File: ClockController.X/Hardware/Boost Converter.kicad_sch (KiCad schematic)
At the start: 9 parts, among them J2 HDR-1X2H, Q2 FDD7N25LZTM, Q3 MMBT2222A-TP, Q4 MMBT2907ALT1G

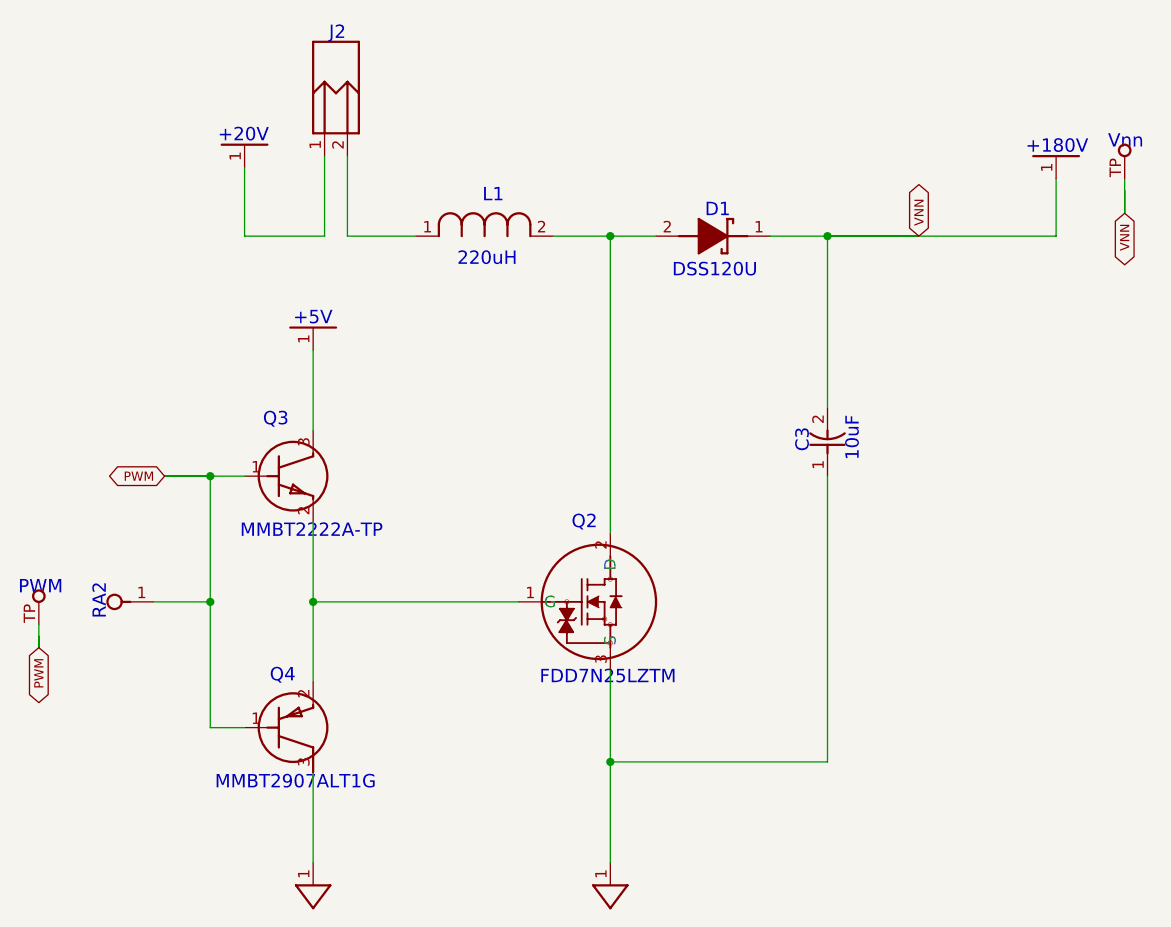
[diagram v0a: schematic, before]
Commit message: Replace the imported objects with native kicad equivalents
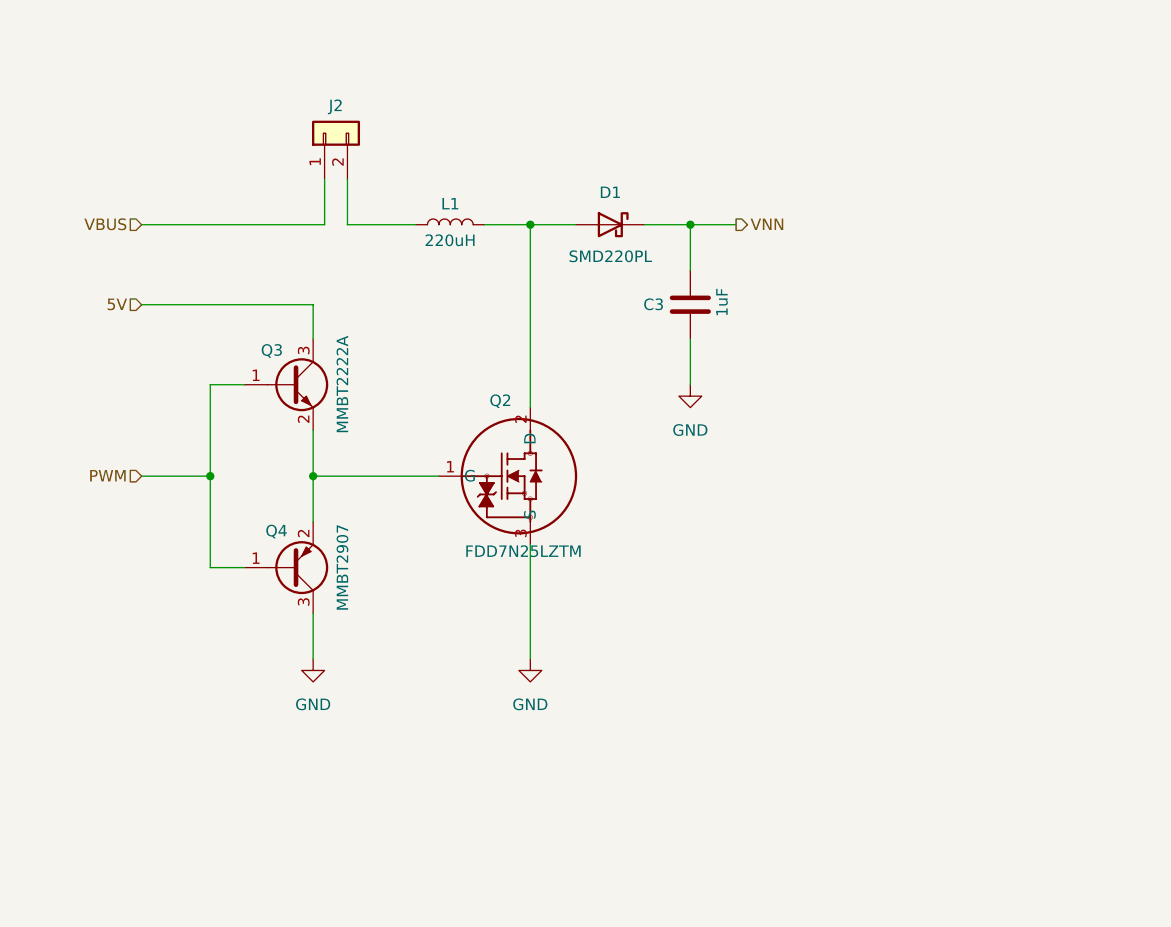
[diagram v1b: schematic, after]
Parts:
- removed PWM0, Vnn0: Most Density, Clock Controller:TP_1.25MM, symbol Clock Controller-eagle-import:TP_1.25MM
- C3: value 10uF -> 1uF; symbol Clock Controller-eagle-import:CAP_1206 -> Device:C
- D1: symbol Clock Controller-eagle-import:DSS120U -> Device:D_Schottky
- J2: symbol Clock Controller-eagle-import:HDR-1X2H -> Connector_Generic:Conn_01x02
- L1: footprint Clock Controller:SRN8040TA221M -> Inductor_:SRN8040TA221M; symbol Clock Controller-eagle-import:SRN8040TA-221M -> Device:L
- Q3: value MMBT2222A-TP -> MMBT2222A; symbol Clock Controller-eagle-import:MMBT2222A-TP -> Transistor_BJT:MMBT2222A
- Q4: value MMBT2907ALT1G -> MMBT2907; symbol Clock Controller-eagle-import:MMBT2907ALT1G -> Transistor_BJT:Q_PNP_BEC
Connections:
- net GND_DIGITAL is gone; now on net GND: C3.1, Q2.3 (S)
- net GND: now reaches Q4.3 (C)
- net +180V renamed VNN
- net +20V renamed VBUS
- net +5V renamed 5V
- net RA2 renamed PWM
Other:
- note removed: "+180V"
- note removed: "+20V"
- note removed: "+5V"
- note removed: "10uF"
- note removed: "220uH"
- note removed: "C3"
- note removed: "D1"
- note removed: "DSS120U"
- note removed: "FDD7N25LZTM"
- note removed: "J2"
- note removed: "L1"
- note removed: "MMBT2222A-TP"
- note removed: "MMBT2907ALT1G"
- note removed: "PWM"
- note removed: "Q2"
- note removed: "Q3"
- note removed: "Q4"
- note removed: "RA2"
- note removed: "Vnn"

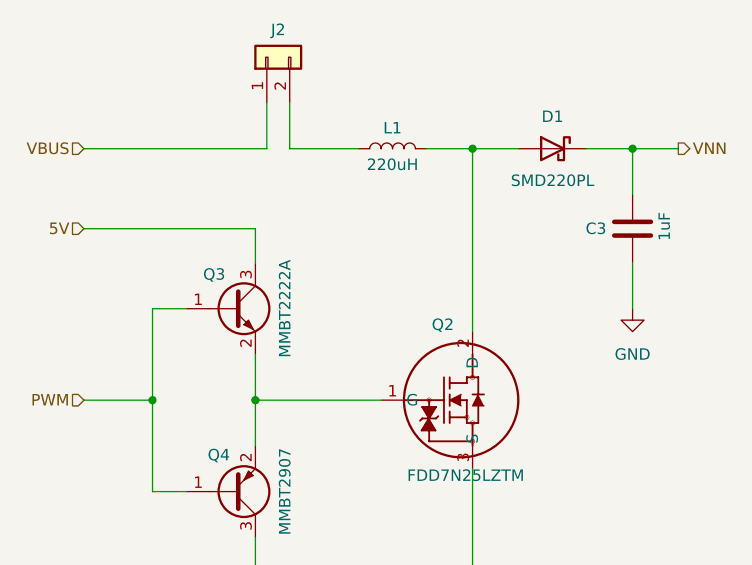
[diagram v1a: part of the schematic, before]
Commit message: Named all nets
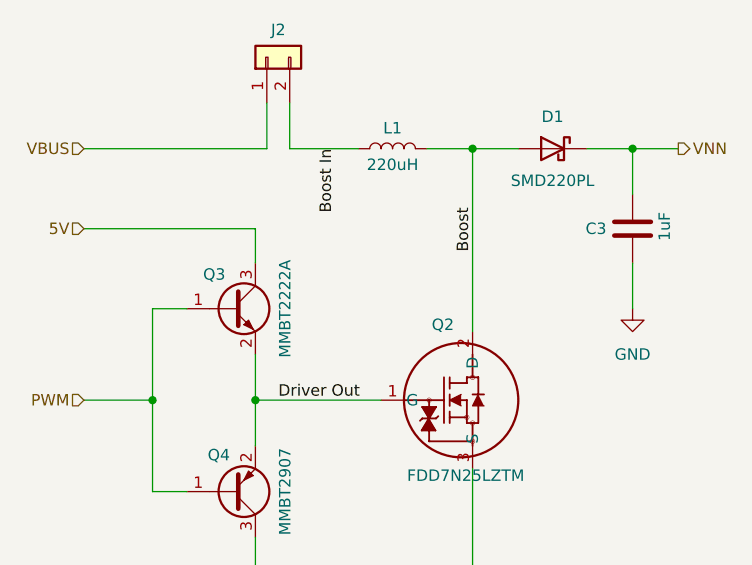
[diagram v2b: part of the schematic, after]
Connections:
- net Boost In: now reaches J2.2 (Pin_2), L1.1
- net Boost: now reaches D1.2 (A), L1.2, Q2.2 (D)
- net Driver Out: now reaches Q2.1 (G), Q3.2 (E), Q4.2 (E)
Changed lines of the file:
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@@
+		)
+	)
+	(label "Driver Out"
+		(at 118.11 104.14 0)
+		(effects
+			(font
+				(size 1.27 1.27)
+			)
+			(justify left bottom)
+		)
+	)
+	(label "Boost"
+		(at 139.7 87.63 90)
+		(effects
+			(font
+				(size 1.27 1.27)
+			)
+			(justify left bottom)
+		)
+	)
+	(label "Boost In"
+		(at 124.46 76.2 270)
+		(effects
+			(font
+				(size 1.27 1.27)
+			)
+			(justify right bottom)
 		)
 	)
@@
 		)
 		(instances
-			(project ""
+			(project "Clock Controller"
 				(path "/de4049ea-1674-4dcc-86d3-bb1be3dcf2e7/44189c1c-ba8e-4c06-ad6c-4084ba07d9ce"
 					(reference "#PWR015")
@@
 		)
 		(instances
-			(project ""
+			(project "Clock Controller"
 				(path "/de4049ea-1674-4dcc-86d3-bb1be3dcf2e7/44189c1c-ba8e-4c06-ad6c-4084ba07d9ce"
 					(reference "#PWR014")

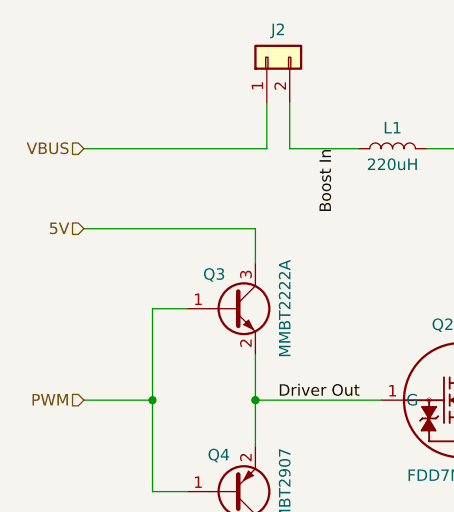
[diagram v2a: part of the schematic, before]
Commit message: Converting to single board layout
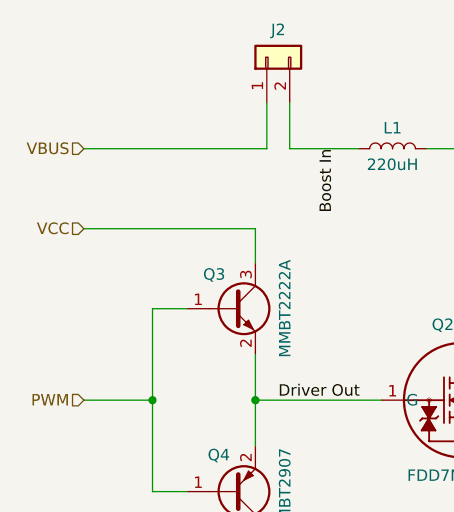
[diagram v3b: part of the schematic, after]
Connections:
- net 5V renamed VCC
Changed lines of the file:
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@@
 	(generator "eeschema")
 	(generator_version "9.0")
-	(paper "A4")
+	(paper "USLetter")
 	(junction
 		(at 104.14 104.14)
@@
 	(wire
 		(pts
+			(xy 157.48 76.2) (xy 162.56 76.2)
+		)
+		(stroke
+			(width 0)
+			(type default)
+		)
+	)
+	(wire
+		(pts
+			(xy 115.57 119.38) (xy 115.57 124.46)
+		)
+		(stroke
+			(width 0)
+			(type default)
+		)
+	)
+	(wire
+		(pts
+			(xy 104.14 93.98) (xy 107.95 93.98)
+		)
+		(stroke
+			(width 0)
+			(type default)
+		)
+	)
+	(wire
+		(pts
+			(xy 96.52 85.09) (xy 115.57 85.09)
+		)
+		(stroke
+			(width 0)
+			(type default)
+		)
+	)
+	(wire
+		(pts
+			(xy 152.4 76.2) (xy 157.48 76.2)
+		)
+		(stroke
+			(width 0)
+			(type default)
+		)
+	)
+	(wire
+		(pts
+			(xy 134.62 76.2) (xy 139.7 76.2)
+		)
+		(stroke
+			(width 0)
+			(type default)
+		)
+	)
+	(wire
+		(pts
+			(xy 157.48 76.2) (xy 157.48 81.28)
+		)
+		(stroke
+			(width 0)
+			(type default)
+		)
+	)
+	(wire
+		(pts
+			(xy 115.57 104.14) (xy 129.54 104.14)
+		)
+		(stroke
+			(width 0)
+			(type default)
+		)
+	)
+	(wire
+		(pts
+			(xy 139.7 76.2) (xy 139.7 96.52)
+		)
+		(stroke
+			(width 0)
+			(type default)
+		)
+	)
+	(wire
+		(pts
+			(xy 104.14 114.3) (xy 104.14 104.14)
+		)
+		(stroke
+			(width 0)
+			(type default)
+		)
+	)
+	(wire
+		(pts
+			(xy 139.7 111.76) (xy 139.7 124.46)
+		)
+		(stroke
+			(width 0)
+			(type default)
+		)
+	)
+	(wire
+		(pts
+			(xy 116.84 71.12) (xy 116.84 76.2)
+		)
+		(stroke
+			(width 0)
+			(type default)
+		)
+	)
+	(wire
+		(pts
+			(xy 119.38 76.2) (xy 127 76.2)
+		)
+		(stroke
+			(width 0)
+			(type default)
+		)
+	)
+	(wire
+		(pts
 			(xy 119.38 71.12) (xy 119.38 76.2)
-		)
-		(stroke
-			(width 0)
-			(type default)
-		)
-	)
-	(wire
-		(pts
-			(xy 157.48 76.2) (xy 162.56 76.2)
-		)
-		(stroke
-			(width 0)
-			(type default)
-		)
-	)
-	(wire
-		(pts
-			(xy 115.57 119.38) (xy 115.57 124.46)
-		)
-		(stroke
-			(width 0)
-			(type default)
-		)
-	)
-	(wire
-		(pts
-			(xy 104.14 93.98) (xy 107.95 93.98)
-		)
-		(stroke
-			(width 0)
-			(type default)
-		)
-	)
-	(wire
-		(pts
-			(xy 96.52 85.09) (xy 115.57 85.09)
-		)
-		(stroke
-			(width 0)
-			(type default)
-		)
-	)
-	(wire
-		(pts
-			(xy 152.4 76.2) (xy 157.48 76.2)
-		)
-		(stroke
-			(width 0)
-			(type default)
-		)
-	)
-	(wire
-		(pts
-			(xy 134.62 76.2) (xy 139.7 76.2)
-		)
-		(stroke
-			(width 0)
-			(type default)
-		)
-	)
-	(wire
-		(pts
-			(xy 157.48 76.2) (xy 157.48 81.28)
-		)
-		(stroke
-			(width 0)
-			(type default)
-		)
-	)
-	(wire
-		(pts
-			(xy 115.57 104.14) (xy 129.54 104.14)
-		)
-		(stroke
-			(width 0)
-			(type default)
-		)
-	)
-	(wire
-		(pts
-			(xy 139.7 76.2) (xy 139.7 96.52)
-		)
-		(stroke
-			(width 0)
-			(type default)
-		)
-	)
-	(wire
-		(pts
-			(xy 104.14 114.3) (xy 104.14 104.14)
-		)
-		(stroke
-			(width 0)
-			(type default)
-		)
-	)
-	(wire
-		(pts
-			(xy 139.7 111.76) (xy 139.7 124.46)
-		)
-		(stroke
-			(width 0)
-			(type default)
-		)
-	)
-	(wire
-		(pts
-			(xy 116.84 71.12) (xy 116.84 76.2)
-		)
-		(stroke
-			(width 0)
-			(type default)
-		)
-	)
-	(wire
-		(pts
-			(xy 119.38 76.2) (xy 127 76.2)
 		)
 		(stroke
@@
 		)
 	)
-	(hierarchical_label "5V"
+	(hierarchical_label "VCC"
 		(shape input)
 		(at 96.52 85.09 180)
@@
 		)
 	)
+	(netclass_flag ""
+		(length 2.54)
+		(shape round)
+		(at 107.95 85.09 0)
+		(fields_autoplaced yes)
+		(effects
+			(font
+				(size 1.27 1.27)
+			)
+			(justify left bottom)
+		)
+		(property "Netclass" "Thicc"
+			(at 108.6485 82.55 0)
+			(effects
+				(font
+					(size 1.27 1.27)
+				)
+				(justify left)
+			)
+		)
+		(property "Component Class" ""
+			(at -81.28 8.89 0)
+			(effects
+				(font
+					(size 1.27 1.27)
+					(italic yes)
+				)
+			)
+		)
+	)
+	(netclass_flag ""
+		(length 2.54)
+		(shape round)
+		(at 139.7 93.98 270)
+		(fields_autoplaced yes)
+		(effects
+			(font
+				(size 1.27 1.27)
+			)
+			(justify right bottom)
+		)
+		(property "Netclass" "Extra Thicc"
+			(at 142.24 93.2815 90)
+			(effects
+				(font
+					(size 1.27 1.27)
+				)
+				(justify left)
+			)
+		)
+		(property "Component Class" ""
+			(at -49.53 17.78 0)
+			(effects
+				(font
+					(size 1.27 1.27)
+					(italic yes)
+				)
+			)
+		)
+	)
+	(netclass_flag ""
+		(length 2.54)
+		(shape round)
+		(at 121.92 104.14 180)
+		(fields_autoplaced yes)
+		(effects
+			(font
+				(size 1.27 1.27)
+			)
+			(justify right bottom)
+		)
+		(property "Netclass" "Thicc"
+			(at 122.6185 106.68 0)
+			(effects
+				(font
+					(size 1.27 1.27)
+				)
+				(justify left)
+			)
+		)
+		(property "Component Class" ""
+			(at -67.31 27.94 0)
+			(effects
+				(font
+					(size 1.27 1.27)
+					(italic yes)
+				)
+			)
+		)
+	)
+	(netclass_flag ""
+		(length 2.54)
+		(shape round)
+		(at 101.6 76.2 0)
+		(fields_autoplaced yes)
+		(effects
+			(font
+				(size 1.27 1.27)
+			)
+			(justify left bottom)
+		)
+		(property "Netclass" "Extra Thicc"
+			(at 102.2985 73.66 0)
+			(effects
+				(font
+					(size 1.27 1.27)
+				)
+				(justify left)
+			)
+		)
+		(property "Component Class" ""
+			(at -87.63 0 0)
+			(effects
+				(font
+					(size 1.27 1.27)
+					(italic yes)
+				)
+			)
+		)
+	)
+	(netclass_flag ""
+		(length 2.54)
+		(shape round)
+		(at 119.38 71.12 270)
+		(effects
+			(font
+				(size 1.27 1.27)
+			)
+			(justify right bottom)
+		)
+		(property "Netclass" "Extra Thicc"
+			(at 123.19 71.12 0)
+			(effects
+				(font
+					(size 1.27 1.27)
+				)
+				(justify left)
+			)
+		)
+		(property "Component Class" ""
+			(at -13.97 3.81 0)
+			(effects
+				(font
+					(size 1.27 1.27)
+					(italic yes)
+				)
+			)
+		)
+	)
+	(netclass_flag ""
+		(length 2.54)
+		(shape round)
+		(at 154.94 76.2 0)
+		(fields_autoplaced yes)
+		(effects
+			(font
+				(size 1.27 1.27)
+			)
+			(justify left bottom)
+		)
+		(property "Netclass" "VNN"
+			(at 155.6385 73.66 0)
+			(effects
+				(font
+					(size 1.27 1.27)
+				)
+				(justify left)
+			)
+		)
+		(property "Component Class" ""
+			(at -34.29 -1.27 0)
+			(effects
+				(font
+					(size 1.27 1.27)
+					(italic yes)
+				)
+			)
+		)
+	)
